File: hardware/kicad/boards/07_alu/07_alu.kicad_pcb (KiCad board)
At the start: 2 copper layers, 99.8 x 99.7 mm, 187 parts, among them J10 Conn_01x04_Pin, J11 Conn_01x04_Pin, J12 Conn_01x08_Pin, J15 Conn_01x08_Pin, J16 Conn_01x08_Pin, J17 Conn_01x08_Pin, J5 Conn_01x08_Pin, J6 Conn_01x08_Pin, J7 Conn_01x08_Pin, U1 74AHC541, U16 74ACT151, U3 74ACT283, U36 74HC86, U37 74LS08, U38 74LS540, U4 74HC688, U40 74LS377, U41 74ACT151, U42 74ACT151, U43 74ACT151, U44 74ACT151, U45 74ACT151, U46 74ACT151, U47 74ACT151, U48 74ACT151, U49 74ACT151, U5 74ACT283, U50 74ACT151, U51 74ACT151, U52 74ACT151, U53 74ACT151, U54 74ACT151, U55 74ACT151, U56 74ACT151

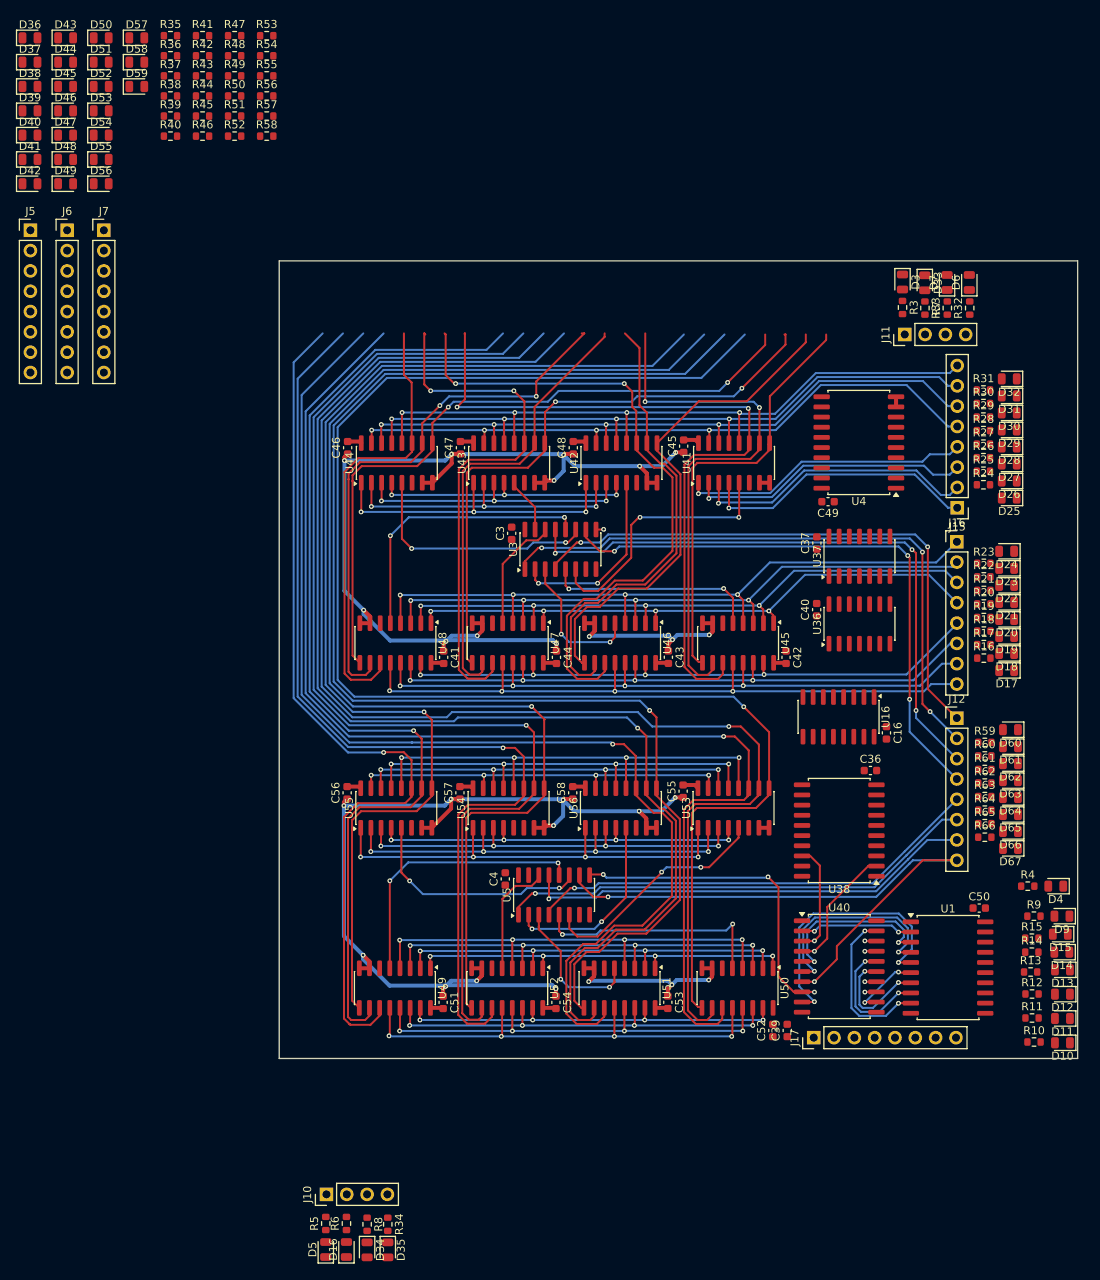
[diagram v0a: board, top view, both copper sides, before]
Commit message: checkpoint: routed all but 60 traces
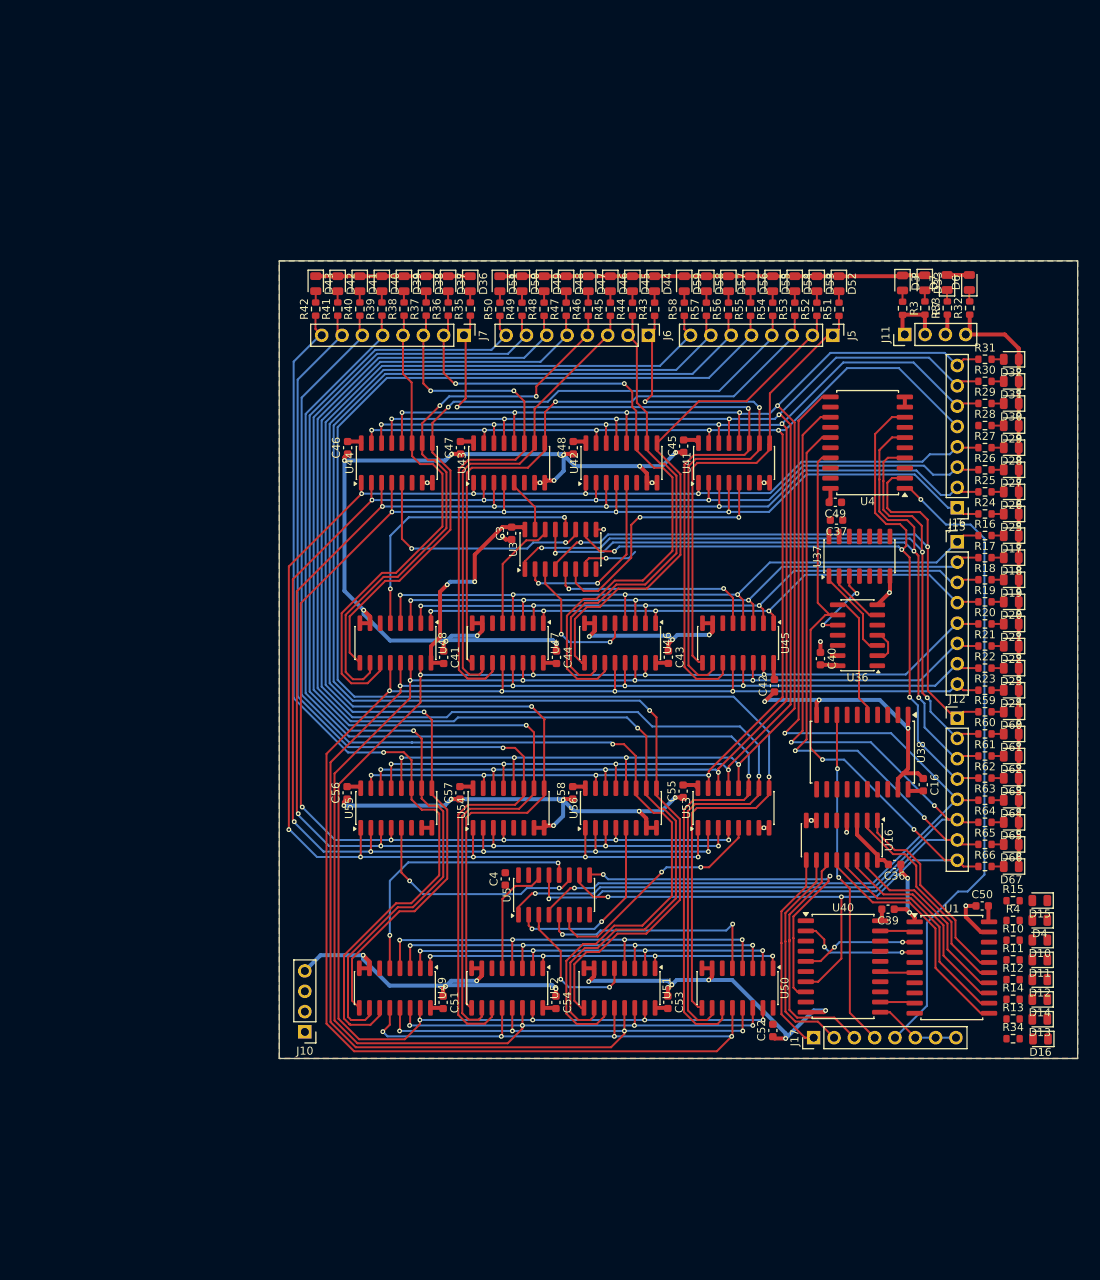
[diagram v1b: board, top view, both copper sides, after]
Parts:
- removed D34, D35, D5, D9: LED, LED_SMD:LED_0805_2012Metric
- removed R5, R6, R8: 330 Ohm, Resistor_SMD:R_0603_1608Metric
- removed R9: 330, Resistor_SMD:R_0603_1608Metric
- R34: value 330 Ohm -> 330
- moved J5 101.2 mm to (131.4, 52.6), turned to -90 degrees
- moved D52 95.4 mm to (132.2, 46.2), turned to -90 degrees
- moved D53 92.0 mm to (129.4, 46.2), turned to -90 degrees
- moved D16 90.7 mm to (157.4, 140.6), turned to 180 degrees
- moved D54 88.7 mm to (126.6, 46.2), turned to -90 degrees
- moved D55 85.4 mm to (123.9, 46.2), turned to -90 degrees
- moved D56 82.1 mm to (121.1, 46.2), turned to -90 degrees
- moved R34 81.5 mm to (153.9, 140.5), turned to 0 degrees
- moved D57 80.1 mm to (118.3, 46.2), turned to -90 degrees
- moved R51 79.3 mm to (132.2, 49.3), turned to 90 degrees
- moved D44 78.6 mm to (109.1, 46.2), turned to -90 degrees
- moved D58 76.4 mm to (115.6, 46.2), turned to -90 degrees
- moved R52 75.9 mm to (129.4, 49.3), turned to 90 degrees
- moved D45 75.0 mm to (106.3, 46.2), turned to -90 degrees
- moved R53 74.3 mm to (126.6, 49.3), turned to 90 degrees
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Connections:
- net Net-(U1-A1) renamed /flags_logic/q1
- R34 pad 1: GND -> flagGTE
- R34 pad 2: Net-(D35-K) -> Net-(D16-A)
- U1 pad 11: flagGTE -> flagV
- U1 pad 12: flagGT -> flagLT
- U1 pad 13: flagLT -> flagGT
- U1 pad 14: flagV -> flagC
- U1 pad 15: flagC -> flagN
- U1 pad 16: flagN -> flagZ
- U1 pad 18: flagZ -> flagGTE
- U1 pad 2: Net-(U1-A0) -> /flags_logic/q7
- U1 pad 4: Net-(U1-A2) -> /flags_logic/q0
- U1 pad 5: Net-(U1-A3) -> /flags_logic/q2
- U1 pad 6: Net-(U1-A4) -> /flags_logic/q3
- U1 pad 7: Net-(U1-A5) -> /flags_logic/q6
- U1 pad 8: Net-(U1-A6) -> /flags_logic/q5
- U1 pad 9: Net-(U1-A7) -> /flags_logic/q4
- U16 pad 12: flagGT -> flagV
- U16 pad 14: flagV -> flagGT
- U16 pad 15: flagN -> flagC
- U16 pad 2: flagC -> flagN
- U40 pad 12: Net-(U1-A4) -> /flags_logic/q4
- U40 pad 15: Net-(U1-A5) -> /flags_logic/q5
- U40 pad 16: Net-(U1-A6) -> /flags_logic/q6
- U40 pad 19: Net-(U1-A7) -> /flags_logic/q7
- U40 pad 2: Net-(U1-A0) -> /flags_logic/q0
- U40 pad 6: Net-(U1-A2) -> /flags_logic/q2
- U40 pad 9: Net-(U1-A3) -> /flags_logic/q3
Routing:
- net GND: track 294.3 -> 509.0 mm, vias 26 -> 76
- net ALU_OPCODE_X7: track 142.7 -> 244.3 mm
- net ALU_OPCODE_X6: track 136.8 -> 224.5 mm
- net ZIN: track 0.00 -> 80.3 mm, vias 0 -> 1
- net ALU_OPCODE_Y0: track 116.2 -> 194.8 mm, vias 8 -> 9
- net ALU_OPCODE_X5: track 130.8 -> 205.9 mm
- net ALU_OPCODE_Y1: track 122.1 -> 196.6 mm, vias 8 -> 9
- net OUT4: track 57.3 -> 130.1 mm, vias 1 -> 2
- net OUT5: track 60.3 -> 131.5 mm, vias 1 -> 3
- net ALU_OPCODE_Y2: track 126.8 -> 196.7 mm, vias 8 -> 9
- net OUT6: track 57.0 -> 126.5 mm, vias 1 -> 3
- net ALU_OPCODE_Y3: track 132.1 -> 198.1 mm, vias 8 -> 9
- net ALU_OPCODE_X4: track 124.9 -> 187.3 mm
- net OUT7: track 77.4 -> 138.3 mm, vias 2 -> 4
- net VCC: track 25.8 -> 79.6 mm, vias 0 -> 2
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- added copper zone on B.Cu, net GND
- added copper zone on F.Cu, net VCC

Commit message: feat: routed final board 🎉
Area: 100mm by 100mm
Layer: 2 layers
Power trace: 0.5mm
Default trace: 0.25mm
Clearance: 0.25mm
DRC: 4 drc thermal errors after routing and pending resolution
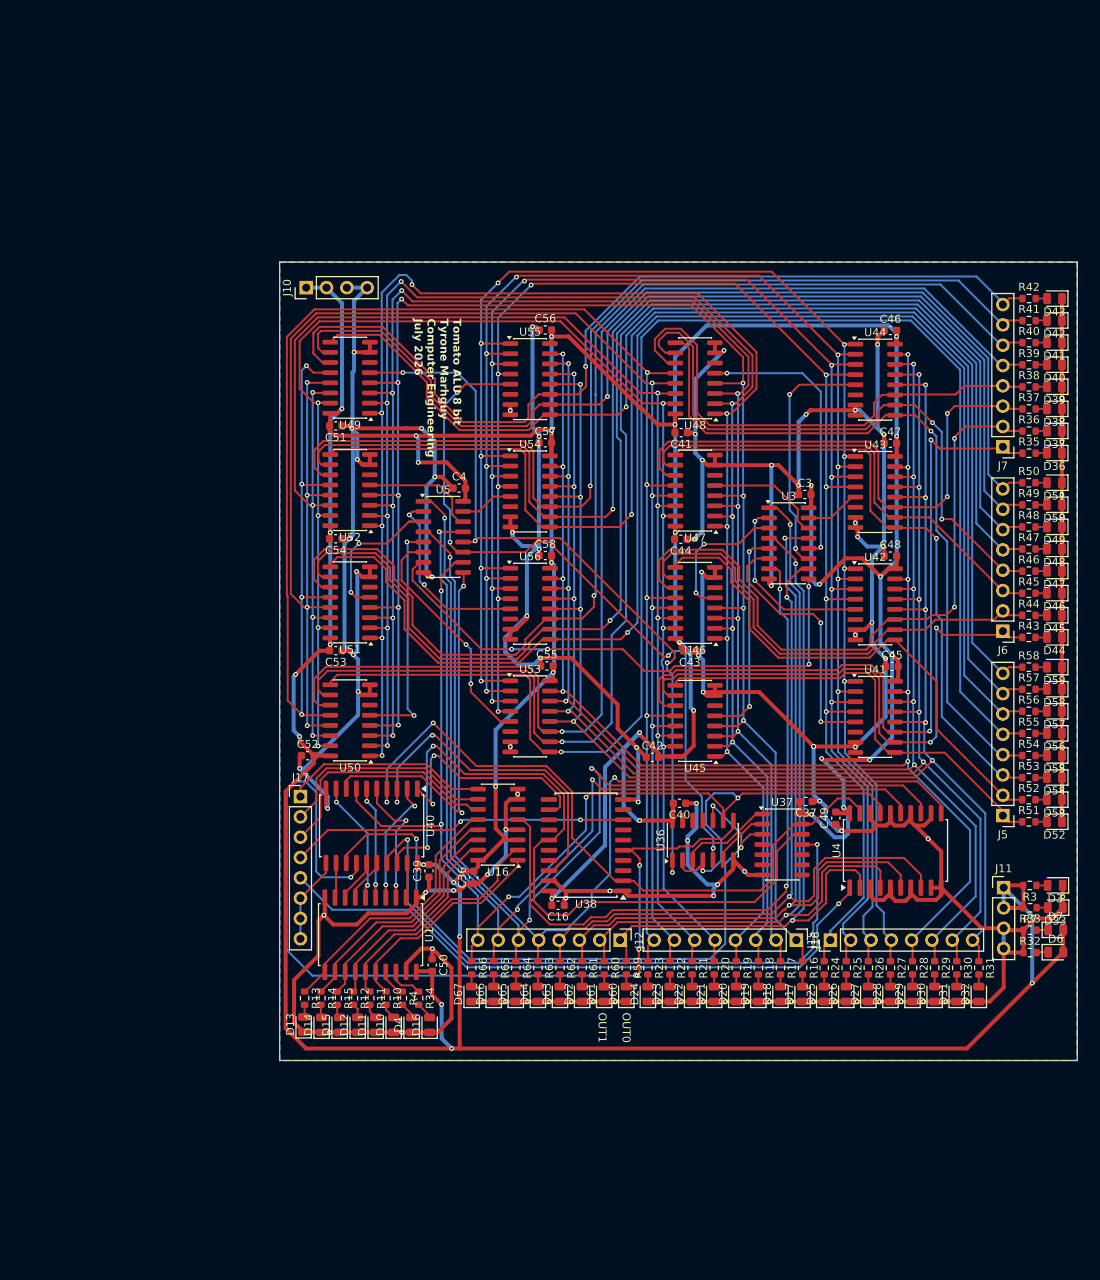
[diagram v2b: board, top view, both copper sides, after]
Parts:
- moved J10 93.0 mm to (65.6, 46.6), turned to 90 degrees
- moved D43 92.4 mm to (159.1, 48.0), turned to 180 degrees
- moved D13 92.0 mm to (65.2, 138.8), turned to 90 degrees
- moved D14 89.8 mm to (67.5, 138.8), turned to 90 degrees
- moved D42 89.7 mm to (159.1, 50.8), turned to 180 degrees
- moved R42 89.2 mm to (155.9, 48.0), turned to 0 degrees
- moved D15 88.9 mm to (69.8, 138.8), turned to 90 degrees
- moved R13 88.6 mm to (65.4, 135.5), turned to -90 degrees
- moved D41 87.1 mm to (159.1, 53.5), turned to 180 degrees
- moved R14 86.5 mm to (67.4, 135.5), turned to -90 degrees
- moved R41 86.4 mm to (155.9, 50.8), turned to 0 degrees
- moved D12 85.5 mm to (72.0, 138.8), turned to 90 degrees
- moved R15 85.4 mm to (69.4, 135.5), turned to -90 degrees
- moved D40 84.7 mm to (159.1, 56.3), turned to 180 degrees
- moved D6 84.4 mm to (159.2, 129.7), turned to 0 degrees
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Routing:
- net VCC: track 79.6 -> 692.6 mm, vias 2 -> 35
- net GND: track 509.0 -> 800.8 mm, vias 76 -> 95
- net LT-SIGN: track 15.9 -> 118.5 mm, vias 0 -> 4
- net GTE-SIGN: track 0.00 -> 93.5 mm, vias 0 -> 2
- net ~ZOUT: track 0.00 -> 87.6 mm, vias 0 -> 2
- net GT-SIGN: track 0.00 -> 81.8 mm, vias 0 -> 2
- net CIN-MAIN: track 8.60 -> 88.3 mm, vias 1 -> 2
- net ALU_OPCODE_X3: track 127.2 -> 203.9 mm, vias 8 -> 9
- net VOUT: track 10.3 -> 86.6 mm, vias 2 -> 3
- net ALU_OPCODE_X2: track 133.0 -> 204.0 mm, vias 8 -> 9
- net /alu_4b_0/cout: track 1.04 -> 68.5 mm, vias 1 -> 4
- net ALU_OPCODE_X1: track 139.3 -> 204.7 mm, vias 8 -> 9
- net Beff: track 29.1 -> 91.0 mm, vias 2 -> 4
- net Aeff: track 34.1 -> 95.1 mm, vias 2 -> 4
- net ALU_OPCODE_X0: track 147.0 -> 206.7 mm, vias 8 -> 9
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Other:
- board size 99.8 x 99.7 mm -> 99.7 x 99.8 mm
- board text added: "OUT0"
- board text added: "OUT1"
- board text added: "Tomato ALU 8 bit Tyrone Marhguy Computer Engineering July 2026"

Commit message: fpga: implemented fsm to brute force find matching opcode
It finds opcode by brute force sweeping across 256 by 256 and checking if computed output is equal to expected test output
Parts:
- removed C37: 100nF, Capacitor_SMD:C_0603_1608Metric
- removed U37: 74LS08, Package_SO:SOIC-14_3.9x8.7mm_P1.27mm
- removed U38: 74LS540, Package_SO:SOIC-20W_7.5x12.8mm_P1.27mm
- added C59: 100nF, Capacitor_SMD:C_0603_1608Metric, F.Cu at (126.6, 110.9)
- added U2: 74HC00, Package_SO:SOIC-14_3.9x8.7mm_P1.27mm, F.Cu at (103.0, 117.8)
- added U6: 74HC00, Package_SO:SOIC-14_3.9x8.7mm_P1.27mm, F.Cu at (124.6, 116.4)
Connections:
- U36 pad 11: unconnected-(U36-Pad11) -> GTE-SIGN
- U36 pad 12: unconnected-(U36-Pad12) -> LT-SIGN
- U36 pad 13: unconnected-(U36-Pad13) -> LT-SIGN
- U36 pad 3: Net-(U36-Pad3) -> /flags_logic/j0
- U36 pad 6: Net-(U36-Pad6) -> /flags_logic/j1
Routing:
- net ~ZOUT: track 87.6 -> 63.2 mm
- net GTE-SIGN: track 93.5 -> 81.1 mm
- net Net-(U36-Pad3): track 11.7 -> 0.00 mm
- net GND: track 800.8 -> 792.7 mm, vias 95 -> 94
- net Net-(U36-Pad6): track 7.32 -> 0.00 mm
- net /flags_logic/j0: track 0.00 -> 5.75 mm
- net FLAG_WE: track 42.3 -> 37.0 mm
- net VCC: track 692.6 -> 689.1 mm
- net VOUT: track 86.6 -> 83.6 mm
- net LT-SIGN: track 118.5 -> 115.4 mm
- net GT-SIGN: track 81.8 -> 79.9 mm
- net /flags_logic/j1: track 0.00 -> 0.97 mm
- net ZOUT: track 42.9 -> 42.4 mm

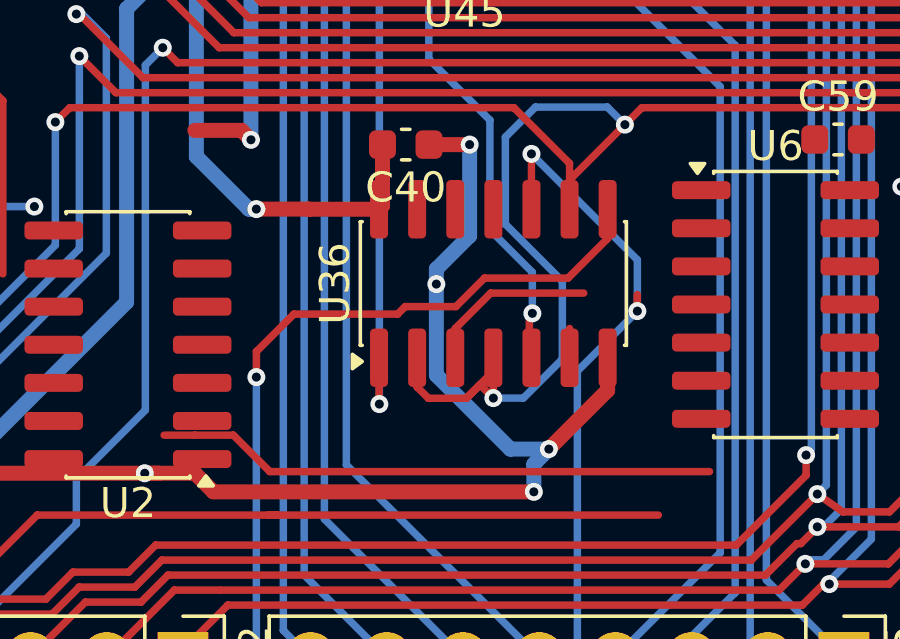
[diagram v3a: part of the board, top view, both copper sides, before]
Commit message: fix: updated the flag logic to match simulation in digital design
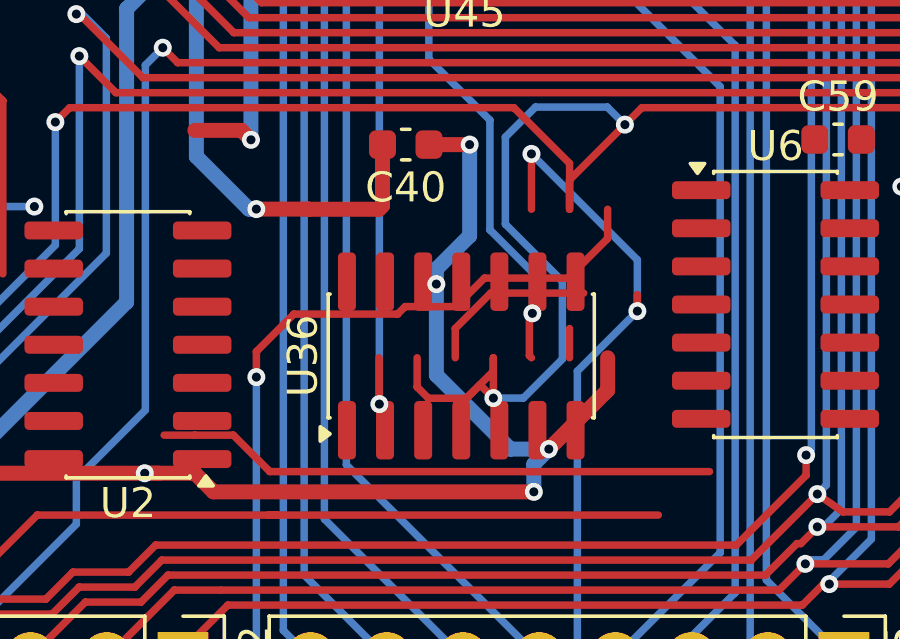
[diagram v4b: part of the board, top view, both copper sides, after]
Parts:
- moved U36 2.64 mm to (114.1, 118.1)
